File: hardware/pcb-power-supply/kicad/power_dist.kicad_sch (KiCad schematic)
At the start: 14 parts, among them U4 MT3608, U5 LR1801G-33-SH2-R

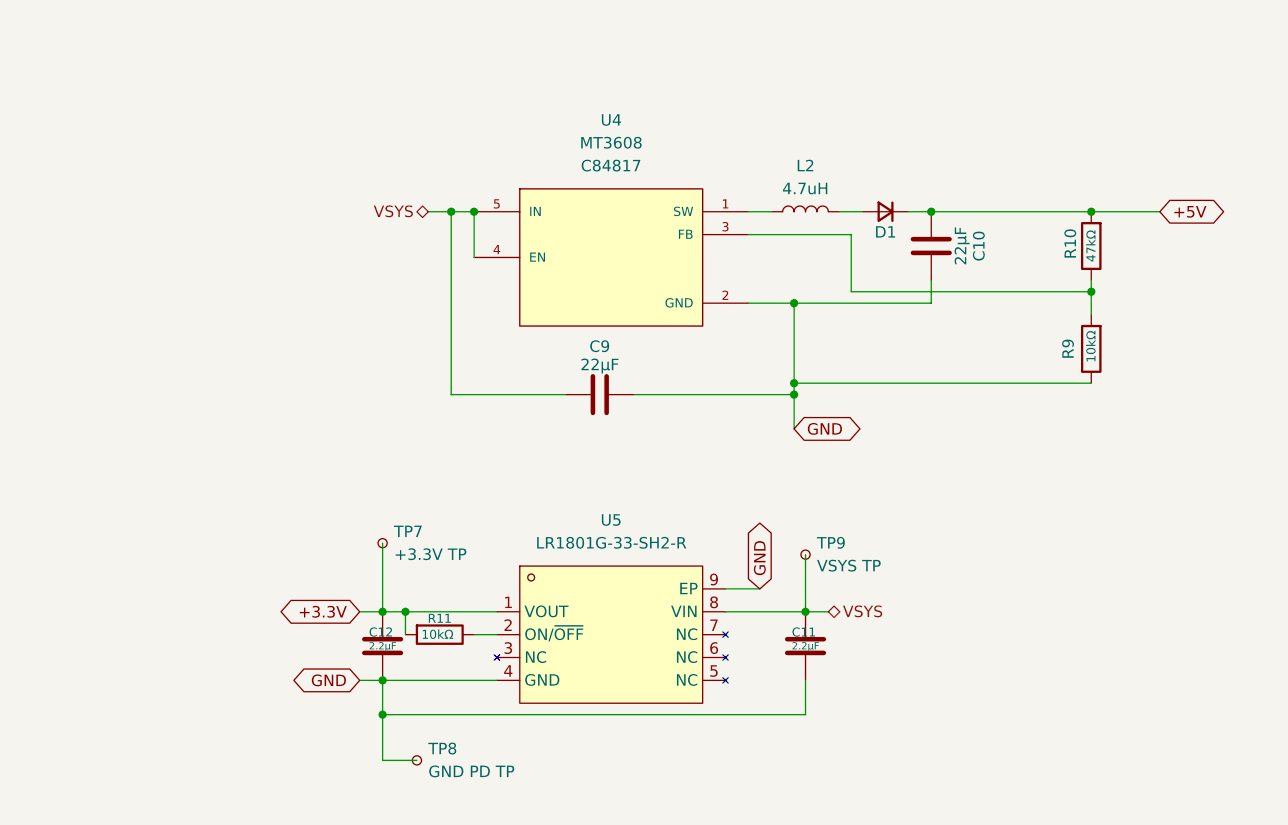
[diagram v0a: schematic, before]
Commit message: Add circuit-context.json for power supply PCB
Extract and annotate schematic context for the power supply board
(50 components, 29 nets, 4 functional blocks across 5 sheets).
Covers USB PD negotiation (STUSB4500), battery management (BQ24195),
power distribution (MT3608 boost + LR1801 LDO), and output connectors.

Creates power-schematic-context initiative docs (BRIEF/PLAN/TASKS).
Component ai_ annotations written to .kicad_sch files via annotate.py;
net/block annotations stored in circuit-context.json.

Made-with: Cursor
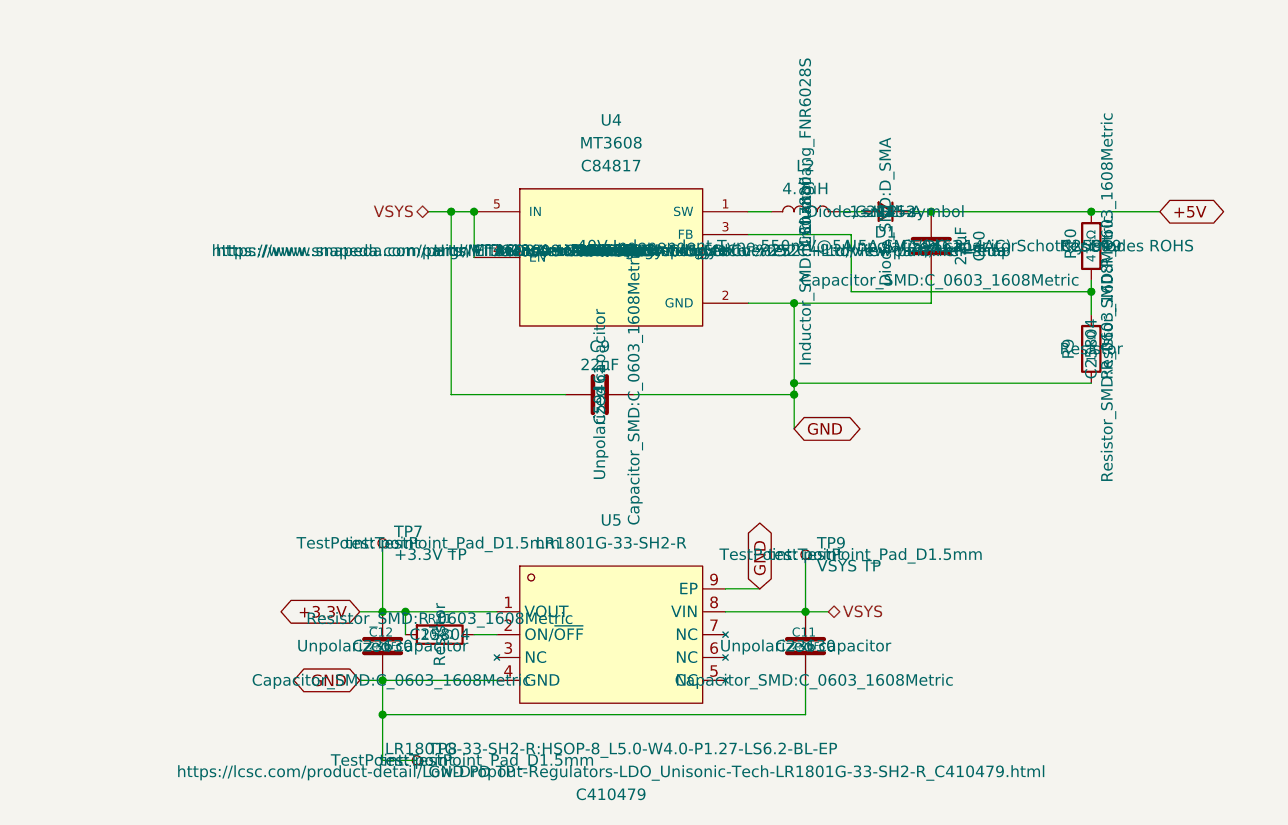
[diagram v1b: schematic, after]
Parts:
- C10: ai_block (none) -> power_dist; ai_critical_specs (none) -> 22uF ceramic; ai_function (none) -> Boost converter +5V output capacitor; ai_role (none) -> decoupling
- C11: ai_block (none) -> power_dist; ai_critical_specs (none) -> 2.2uF ceramic; ai_function (none) -> LR1801 VSYS input capacitor; ai_role (none) -> decoupling
- C12: ai_block (none) -> power_dist; ai_critical_specs (none) -> 2.2uF ceramic; ai_function (none) -> LR1801 +3.3V output capacitor; ai_role (none) -> decoupling
- C9: ai_block (none) -> power_dist; ai_critical_specs (none) -> 22uF ceramic; ai_function (none) -> Boost converter VSYS input capacitor; ai_role (none) -> decoupling
- D1: ai_block (none) -> power_dist; ai_critical_specs (none) -> 40V 5A Schottky SMA; ai_function (none) -> Boost converter output Schottky rectifier diode; ai_role (none) -> rectifier
- L2: ai_block (none) -> power_dist; ai_critical_specs (none) -> 4.7uH FNR6028S; ai_function (none) -> Boost converter energy storage inductor; ai_role (none) -> inductor
- R10: ai_block (none) -> power_dist; ai_critical_specs (none) -> 47k, net labeled +5V but divider targets 3.42V; ai_function (none) -> MT3608 feedback divider top resistor, FB to output; ai_role (none) -> feedback_divider
- R11: ai_block (none) -> power_dist; ai_critical_specs (none) -> 10k; ai_function (none) -> LR1801 ON/OFF enable pull-up to +3.3V output; ai_role (none) -> pull_up
- R9: ai_block (none) -> power_dist; ai_critical_specs (none) -> 10k, Vout=0.6V*(1+Rtop/Rbot)=3.42V with current values; ai_function (none) -> MT3608 feedback divider bottom resistor, FB to GND; ai_role (none) -> feedback_divider
- TP7: ai_block (none) -> power_dist; ai_function (none) -> +3.3V rail test point; ai_role (none) -> test_point
- TP8: ai_block (none) -> power_dist; ai_function (none) -> Ground test point, power distribution; ai_role (none) -> test_point
- TP9: ai_block (none) -> power_dist; ai_function (none) -> VSYS rail test point, power distribution; ai_role (none) -> test_point
- U4: ai_block (none) -> power_dist; ai_critical_specs (none) -> MT3608, 2A switch, up to 24V out; ai_function (none) -> Step-up boost converter, VSYS to +5V output; ai_role (none) -> boost_converter
- U5: ai_block (none) -> power_dist; ai_critical_specs (none) -> LR1801, 1A output, 3.3V fixed; ai_function (none) -> 3.3V LDO linear regulator from VSYS; ai_role (none) -> voltage_regulator
